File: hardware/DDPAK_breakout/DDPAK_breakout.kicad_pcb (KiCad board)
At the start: 2 copper layers, 16.5 x 19.1 mm, 6 parts, among them P1 CONN_1, P2 CONN_2, P3 CONN_1, Q1 IRGS14C40L

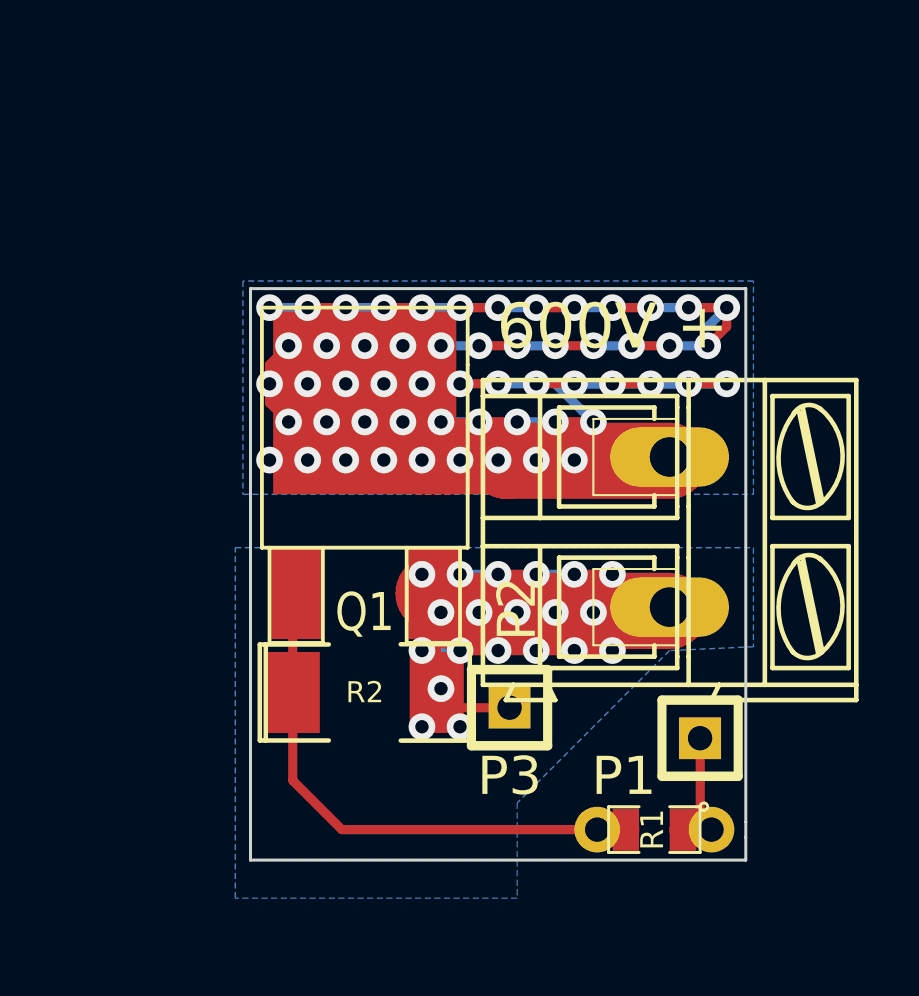
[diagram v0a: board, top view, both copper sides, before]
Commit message: 
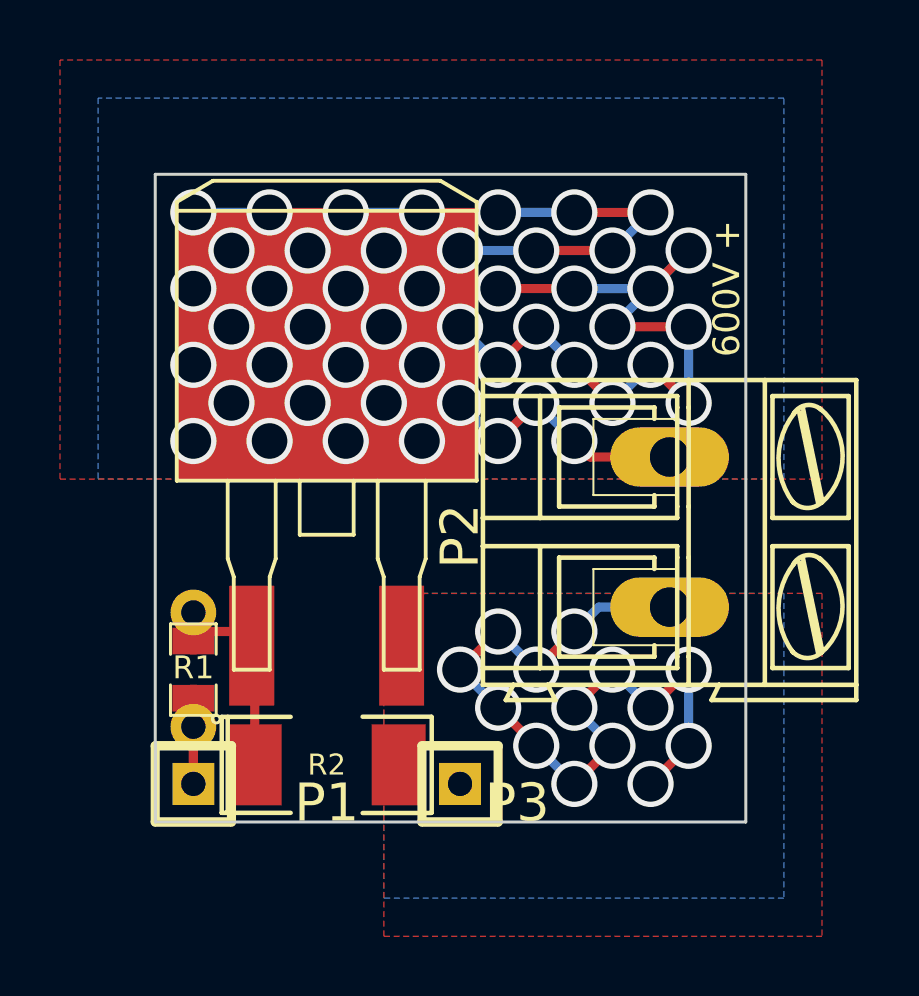
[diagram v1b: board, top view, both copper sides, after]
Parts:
- Q1: footprint DPAK2 -> m-pad-2.1-TO-263AB
- moved P1 17.0 mm to (206.4, 175.3)
- moved R1 16.3 mm to (206.4, 171.4), turned to 90 degrees
- moved Q1 8.35 mm to (210.8, 160.7)
- moved P3 3.03 mm to (215.3, 175.3)
- moved R2 2.73 mm to (210.8, 174.6)
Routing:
- net /GND: track 53.1 -> 27.6 mm, vias 20 -> 14
- net /SIG2: track 17.7 -> 6.29 mm
- net /HV: track 102.2 -> 110.8 mm, vias 56 -> 48
- net /SIG: track 3.28 -> 1.91 mm
- added copper zone on F.Cu, net /GND
- added copper zone on F.Cu, net /HV
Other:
- board size 16.5 x 19.1 mm -> 19.7 x 21.6 mm
- board text added: "rusEFI by DAECU ignition R0.2 DDPAK breakout"
- board text removed: "rusEFI by DAECU ignition R0.1 DDPAK breakout"

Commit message: 
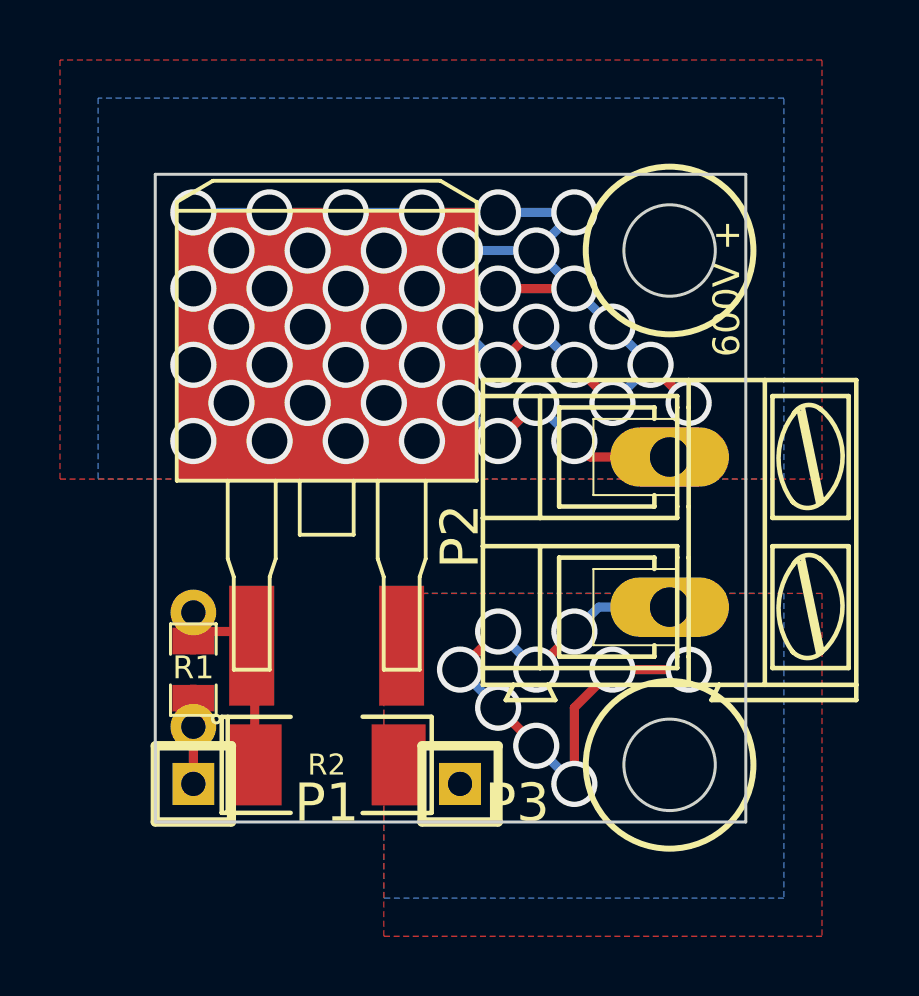
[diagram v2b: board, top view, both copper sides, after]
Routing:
- net /HV: track 110.8 -> 98.1 mm, vias 48 -> 43
- net /GND: track 27.6 -> 21.2 mm, vias 14 -> 9
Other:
- outline, holes or cut-outs redrawn

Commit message: 
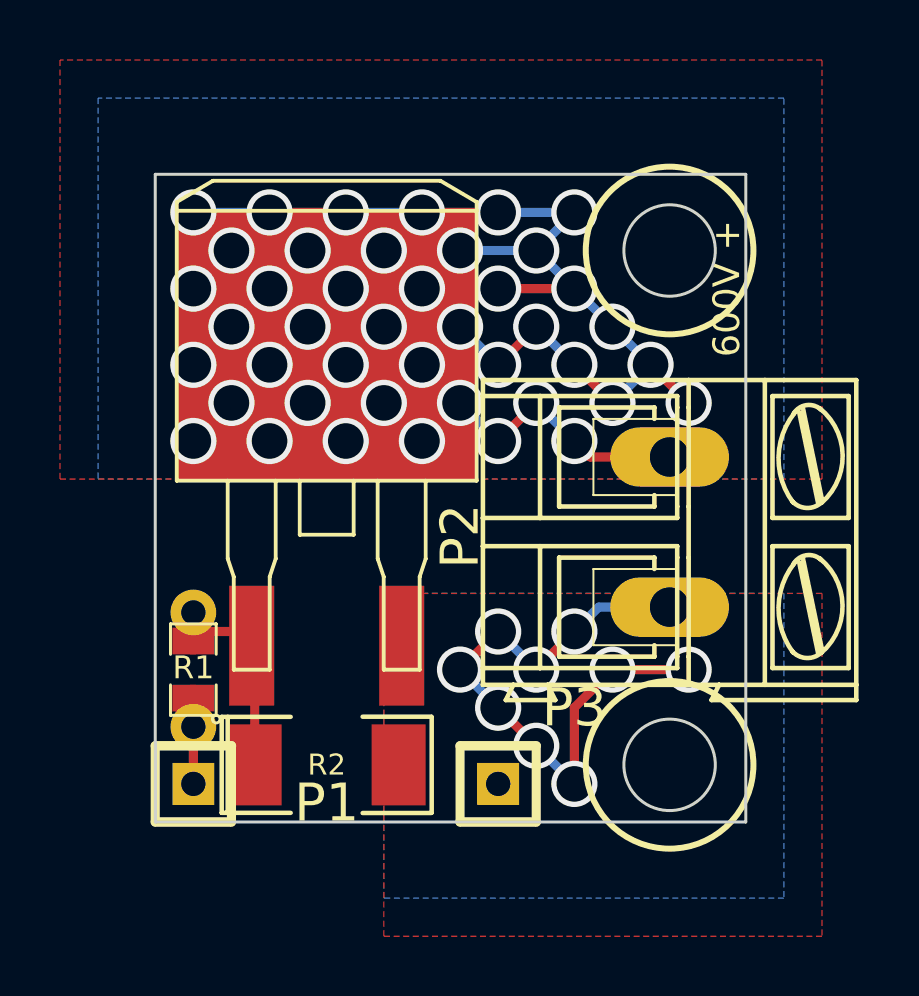
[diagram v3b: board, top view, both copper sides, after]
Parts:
- moved P3 1.27 mm to (216.5, 175.3)
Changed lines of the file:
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@@
     (links 11)
     (no_connects 0)
-    (area 188.850001 145.740001 231.089201 181.229)
+    (area 188.850001 145.740001 231.089201 182.405)
     (thickness 1.6)
-    (drawings 18)
+    (drawings 19)
     (tracks 115)
     (zones 0)
@@
   )
   (module SIL-1 (layer F.Cu)
-    (at 215.265 175.26)
+    (at 216.535 175.26)
     (descr "Connecteurs 1 pin")
     (tags "CONN DEV")
-    (fp_text reference P3 (at 1.905 0.635) (layer F.SilkS)
+    (fp_text reference P3 (at 2.54 -2.54) (layer F.SilkS)
       (effects (font (size 1.27 1.27) (thickness 0.127)))
     )
@@
     )
   )
+  (dimension 10.16 (width 0.3) (layer Dwgs.User)
+    (gr_text "0.4000 in" (at 211.455 181.054999) (layer Dwgs.User)
+      (effects (font (size 1.5 1.5) (thickness 0.3)))
+    )
+    (feature1 (pts (xy 216.535 176.53) (xy 216.535 182.404999)))
+    (feature2 (pts (xy 206.375 176.53) (xy 206.375 182.404999)))
+    (crossbar (pts (xy 206.375 179.704999) (xy 216.535 179.704999)))
+    (arrow1a (pts (xy 216.535 179.704999) (xy 215.408497 180.291419)))
+    (arrow1b (pts (xy 216.535 179.704999) (xy 215.408497 179.118579)))
+    (arrow2a (pts (xy 206.375 179.704999) (xy 207.501503 180.291419)))
+    (arrow2b (pts (xy 206.375 179.704999) (xy 207.501503 179.118579)))
+  )
   (gr_circle (center 222.25 174.625) (end 223.774 174.625) (layer Edge.Cuts) (width 0.1))
